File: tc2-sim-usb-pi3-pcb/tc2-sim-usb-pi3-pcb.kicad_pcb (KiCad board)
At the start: 4 copper layers, 17 x 30 mm, 5 parts, among them J1 Conn_01x08, J2 Conn_01x03

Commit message: v0.4.0
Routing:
- net 4G_USB_D-: track 21.0 -> 21.8 mm
- net 4G_USB_D+: track 20.2 -> 21.0 mm

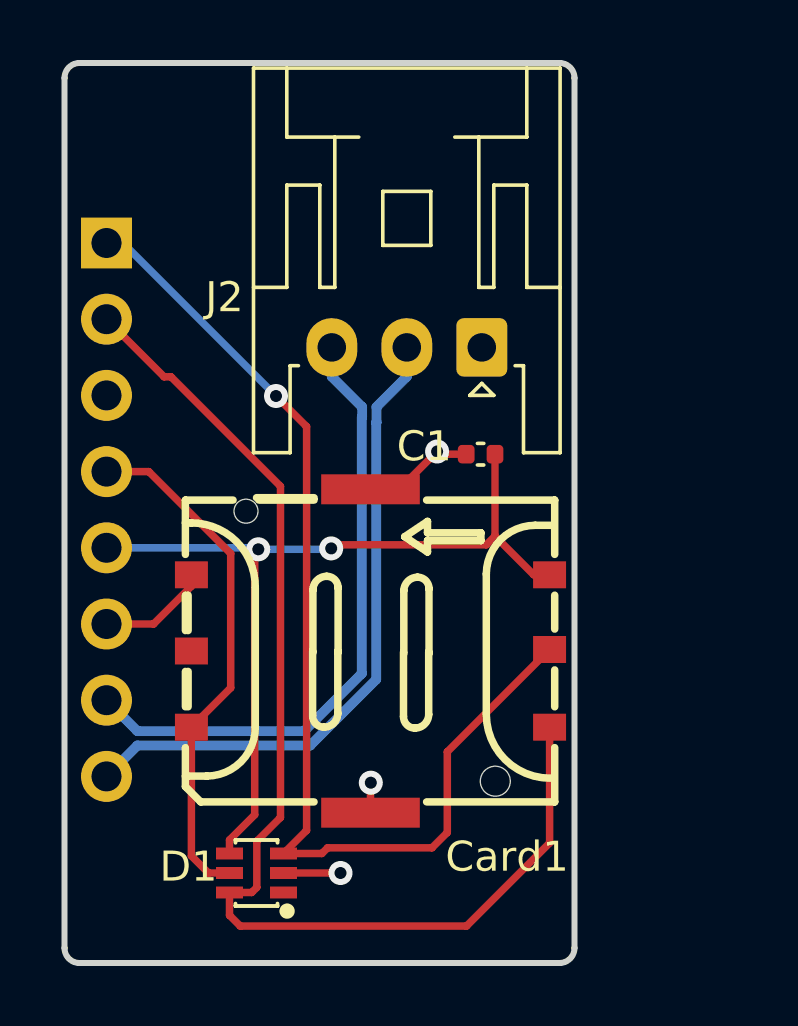
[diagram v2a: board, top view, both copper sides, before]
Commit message: Update to use touch sensor
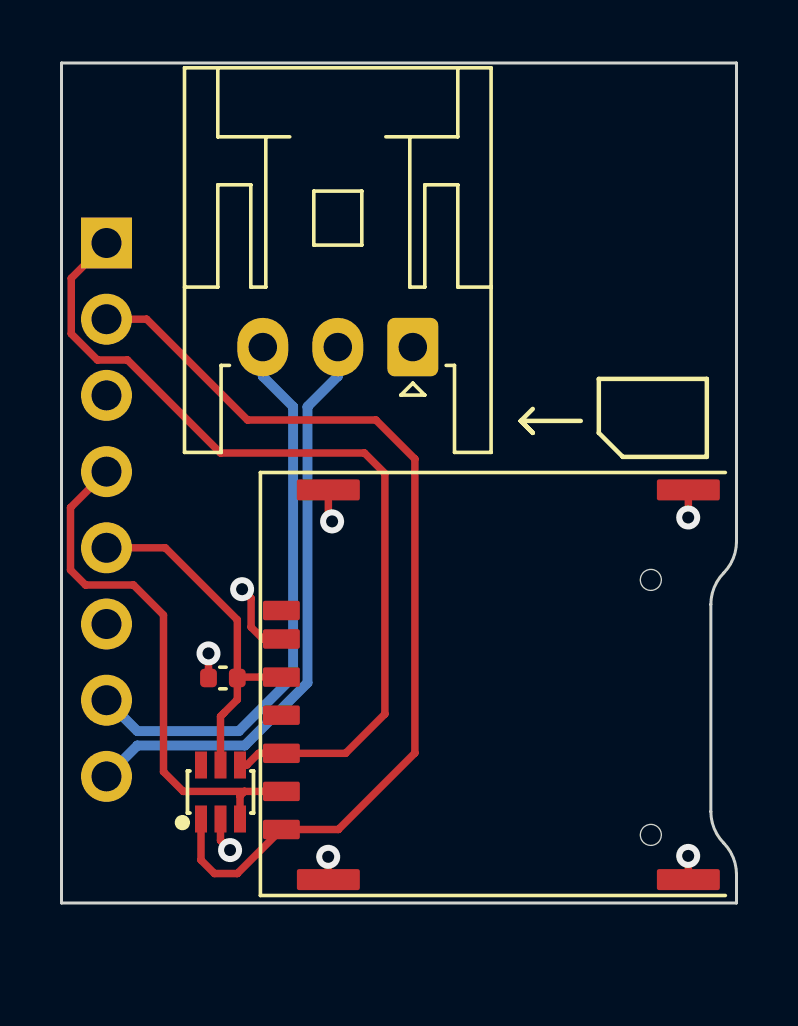
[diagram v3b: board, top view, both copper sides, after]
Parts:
- removed Card1: SIM-Nano, cacophony-library:SIM-SMD_SMN-304
- added U1: ~, cacophony-library:K-DYX-010, F.Cu at (5.83, 19.6)
- moved C1 11.4 mm to (3.88, 14.5)
- moved D1 2.95 mm to (3.80, 18.3), turned to -90 degrees
- moved J2 2.30 mm to (10.2, 3.47)
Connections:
- D1 pad 1: unconnected-(D1-Pad1) -> USIM_CLK
- D1 pad 3: USIM_RST -> USIM_DATA
- D1 pad 4: USIM_VDD -> USIM_RST
- D1 pad 5: USIM_DATA -> USIM_VDD
- D1 pad 6: USIM_CLK -> unconnected-(D1-Pad6)
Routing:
- net USIM_VDD: track 28.8 -> 11.9 mm, vias 2 -> 0
- net USIM_RST: track 37.0 -> 29.5 mm, vias 1 -> 0
- net USIM_CLK: track 39.4 -> 32.4 mm
- net GND: track 10.4 -> 8.13 mm, vias 3 -> 7
- net 4G_USB_D-: track 21.8 -> 19.6 mm
- net 4G_USB_D+: track 21.0 -> 18.8 mm
- net USIM_DATA: track 17.4 -> 17.9 mm
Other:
- board size 17 x 30 mm -> 22.5 x 28 mm
